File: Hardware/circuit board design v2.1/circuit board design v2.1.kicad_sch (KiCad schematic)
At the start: 0 parts

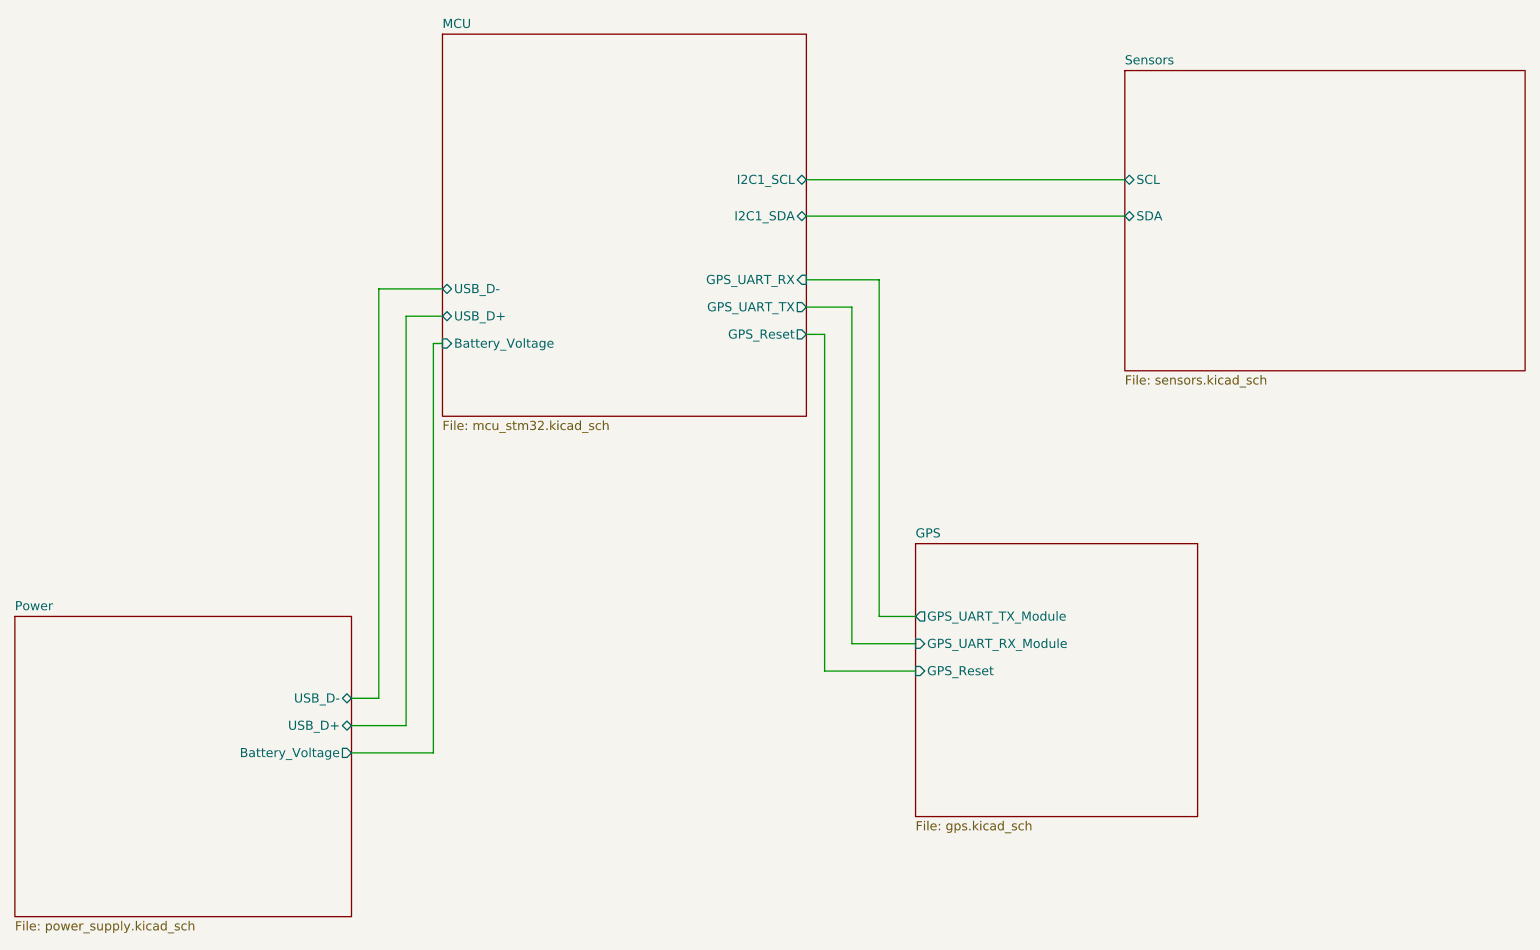
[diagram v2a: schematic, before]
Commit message: Added interupt pins to from BMI088 and LIS
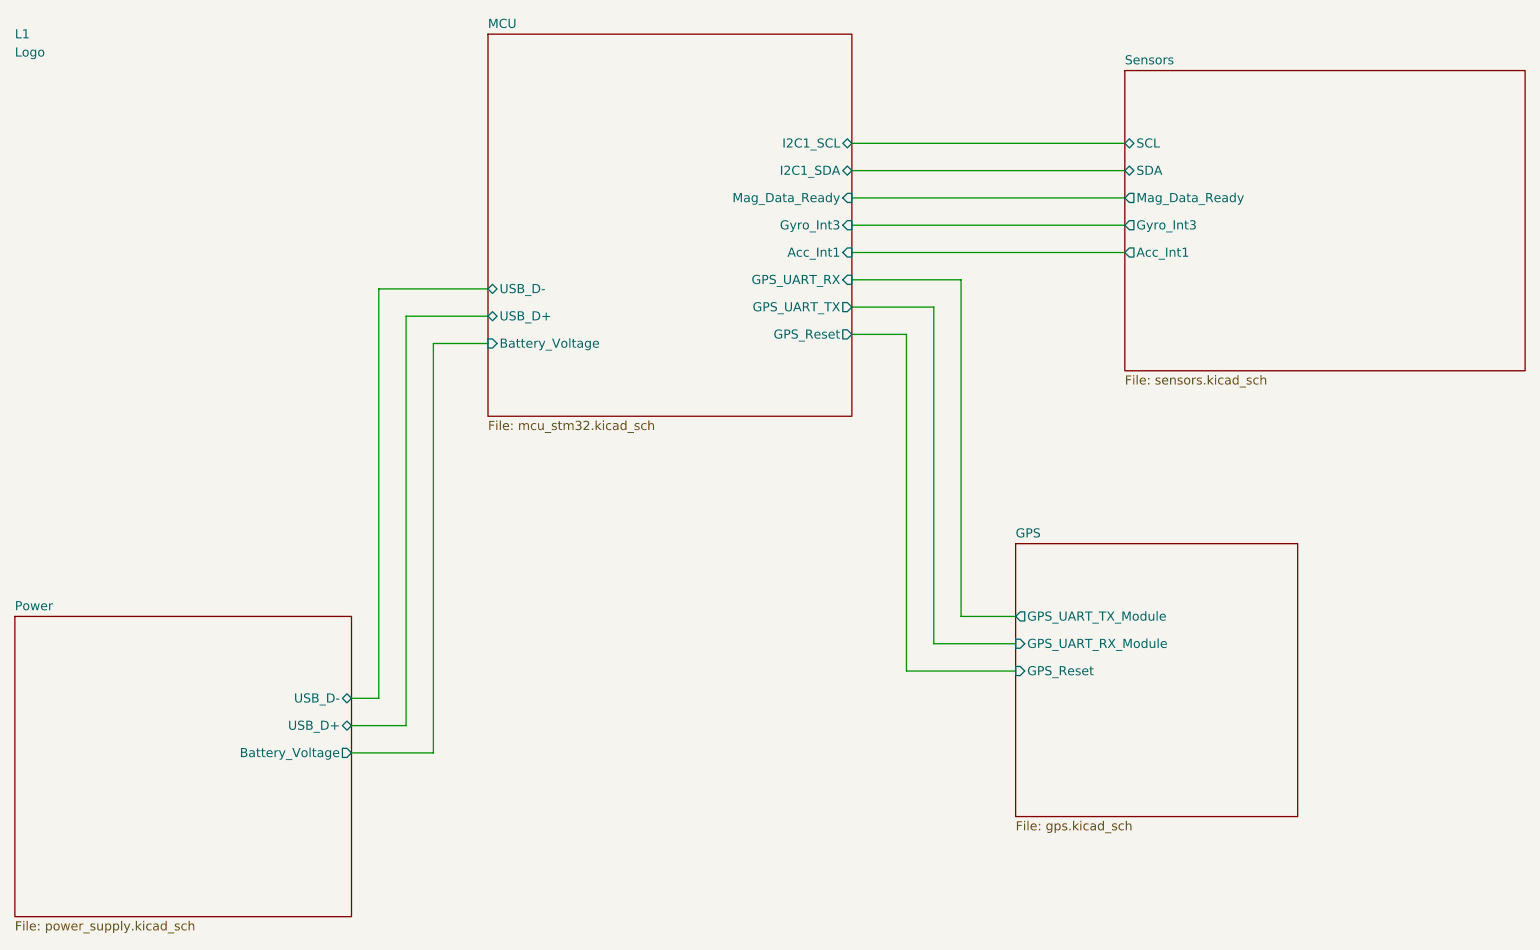
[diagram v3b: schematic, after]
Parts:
- added L1: Logo, Components:ICSS_Logo, symbol Components:Logo
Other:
- sheet MCU ports: added Acc_Int1, Gyro_Int3, Mag_Data_Ready; removed none
- sheet Sensors ports: added Acc_Int1, Gyro_Int3, Mag_Data_Ready; removed none
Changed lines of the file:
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@@
     (stroke (width 0) (type default) (color 0 0 0 0))
   )
-  (wire (pts (xy 144.78 74.93) (xy 144.78 121.92))
-    (stroke (width 0) (type default) (color 0 0 0 0))
-  )
-  (wire (pts (xy 91.44 72.39) (xy 86.36 72.39))
-    (stroke (width 0) (type default) (color 0 0 0 0))
-  )
-  (wire (pts (xy 82.55 68.58) (xy 91.44 68.58))
-    (stroke (width 0) (type default) (color 0 0 0 0))
-  )
-  (wire (pts (xy 148.59 71.12) (xy 148.59 118.11))
+  (wire (pts (xy 156.21 74.93) (xy 156.21 121.92))
+    (stroke (width 0) (type default) (color 0 0 0 0))
+  )
+  (wire (pts (xy 97.79 72.39) (xy 86.36 72.39))
+    (stroke (width 0) (type default) (color 0 0 0 0))
+  )
+  (wire (pts (xy 82.55 68.58) (xy 97.79 68.58))
+    (stroke (width 0) (type default) (color 0 0 0 0))
+  )
+  (wire (pts (xy 160.02 71.12) (xy 160.02 118.11))
     (stroke (width 0) (type default) (color 0 0 0 0))
   )
@@
     (stroke (width 0) (type default) (color 0 0 0 0))
   )
-  (wire (pts (xy 142.24 53.34) (xy 186.69 53.34))
-    (stroke (width 0) (type default) (color 0 0 0 0))
-  )
-  (wire (pts (xy 152.4 114.3) (xy 157.48 114.3))
-    (stroke (width 0) (type default) (color 0 0 0 0))
-  )
-  (wire (pts (xy 142.24 58.42) (xy 186.69 58.42))
+  (wire (pts (xy 163.83 114.3) (xy 171.45 114.3))
     (stroke (width 0) (type default) (color 0 0 0 0))
   )
@@
     (stroke (width 0) (type default) (color 0 0 0 0))
   )
-  (wire (pts (xy 142.24 71.12) (xy 148.59 71.12))
-    (stroke (width 0) (type default) (color 0 0 0 0))
-  )
-  (wire (pts (xy 152.4 67.31) (xy 152.4 114.3))
-    (stroke (width 0) (type default) (color 0 0 0 0))
-  )
-  (wire (pts (xy 148.59 118.11) (xy 157.48 118.11))
-    (stroke (width 0) (type default) (color 0 0 0 0))
-  )
-  (wire (pts (xy 142.24 74.93) (xy 144.78 74.93))
+  (wire (pts (xy 148.59 59.69) (xy 186.69 59.69))
+    (stroke (width 0) (type default) (color 0 0 0 0))
+  )
+  (wire (pts (xy 148.59 71.12) (xy 160.02 71.12))
+    (stroke (width 0) (type default) (color 0 0 0 0))
+  )
+  (wire (pts (xy 163.83 67.31) (xy 163.83 114.3))
+    (stroke (width 0) (type default) (color 0 0 0 0))
+  )
+  (wire (pts (xy 148.59 55.88) (xy 186.69 55.88))
+    (stroke (width 0) (type default) (color 0 0 0 0))
+  )
+  (wire (pts (xy 160.02 118.11) (xy 171.45 118.11))
+    (stroke (width 0) (type default) (color 0 0 0 0))
+  )
+  (wire (pts (xy 148.59 74.93) (xy 156.21 74.93))
+    (stroke (width 0) (type default) (color 0 0 0 0))
+  )
+  (wire (pts (xy 148.59 52.07) (xy 186.69 52.07))
     (stroke (width 0) (type default) (color 0 0 0 0))
   )
@@
     (stroke (width 0) (type default) (color 0 0 0 0))
   )
-  (wire (pts (xy 142.24 67.31) (xy 152.4 67.31))
-    (stroke (width 0) (type default) (color 0 0 0 0))
-  )
-  (wire (pts (xy 90.17 76.2) (xy 91.44 76.2))
-    (stroke (width 0) (type default) (color 0 0 0 0))
-  )
-  (wire (pts (xy 144.78 121.92) (xy 157.48 121.92))
+  (wire (pts (xy 148.59 63.5) (xy 186.69 63.5))
+    (stroke (width 0) (type default) (color 0 0 0 0))
+  )
+  (wire (pts (xy 148.59 67.31) (xy 163.83 67.31))
+    (stroke (width 0) (type default) (color 0 0 0 0))
+  )
+  (wire (pts (xy 90.17 76.2) (xy 97.79 76.2))
+    (stroke (width 0) (type default) (color 0 0 0 0))
+  )
+  (wire (pts (xy 156.21 121.92) (xy 171.45 121.92))
     (stroke (width 0) (type default) (color 0 0 0 0))
   )
   (wire (pts (xy 78.74 133.35) (xy 90.17 133.35))
     (stroke (width 0) (type default) (color 0 0 0 0))
+  )
+  (wire (pts (xy 148.59 48.26) (xy 186.69 48.26))
+    (stroke (width 0) (type default) (color 0 0 0 0))
+  )
+  (symbol (lib_id "Components:Logo") (at 30.48 34.29 0) (unit 1)
+    (in_bom yes) (on_board yes) (fields_autoplaced)
+    (property "Reference" "L1" (id 0) (at 31.75 33.0199 0)
+      (effects (font (size 1.27 1.27)) (justify left))
+    )
+    (property "Value" "Logo" (id 1) (at 31.75 35.5599 0)
+      (effects (font (size 1.27 1.27)) (justify left))
+    )
+    (property "Footprint" "Components:ICSS_Logo" (id 2) (at 30.48 34.29 0)
+      (effects (font (size 1.27 1.27)) hide)
+    )
+    (property "Datasheet" "" (id 3) (at 30.48 34.29 0)
+      (effects (font (size 1.27 1.27)) hide)
+    )
   )
   (sheet (at 186.69 38.1) (size 55.88 41.91) (fields_autoplaced)
@@
       (effects (font (size 1.27 1.27)) (justify left top))
     )
-    (pin "SCL" bidirectional (at 186.69 53.34 180)
-      (effects (font (size 1.27 1.27)) (justify left))
-    )
-    (pin "SDA" bidirectional (at 186.69 58.42 180)
+    (pin "SCL" bidirectional (at 186.69 48.26 180)
+      (effects (font (size 1.27 1.27)) (justify left))
+    )
+    (pin "SDA" bidirectional (at 186.69 52.07 180)
+      (effects (font (size 1.27 1.27)) (justify left))
+    )
+    (pin "Mag_Data_Ready" output (at 186.69 55.88 180)
+      (effects (font (size 1.27 1.27)) (justify left))
+    )
+    (pin "Acc_Int1" output (at 186.69 63.5 180)
+      (effects (font (size 1.27 1.27)) (justify left))
+    )
+    (pin "Gyro_Int3" output (at 186.69 59.69 180)
       (effects (font (size 1.27 1.27)) (justify left))
     )
@@
     )
   )
-  (sheet (at 157.48 104.14) (size 39.37 38.1) (fields_autoplaced)
+  (sheet (at 171.45 104.14) (size 39.37 38.1) (fields_autoplaced)
     (stroke (width 0.1524) (type solid) (color 0 0 0 0))
     (fill (color 0 0 0 0.0000))
-    (property "Sheet name" "GPS" (id 0) (at 157.48 103.4284 0)
+    (property "Sheet name" "GPS" (id 0) (at 171.45 103.4284 0)
       (effects (font (size 1.27 1.27)) (justify left bottom))
     )
-    (property "Sheet file" "gps.kicad_sch" (id 1) (at 157.48 142.8246 0)
+    (property "Sheet file" "gps.kicad_sch" (id 1) (at 171.45 142.8246 0)
       (effects (font (size 1.27 1.27)) (justify left top))
     )
-    (pin "GPS_Reset" input (at 157.48 121.92 180)
-      (effects (font (size 1.27 1.27)) (justify left))
-    )
-    (pin "GPS_UART_TX_Module" output (at 157.48 114.3 180)
-      (effects (font (size 1.27 1.27)) (justify left))
-    )
-    (pin "GPS_UART_RX_Module" input (at 157.48 118.11 180)
-      (effects (font (size 1.27 1.27)) (justify left))
-    )
-  )
-  (sheet (at 91.44 33.02) (size 50.8 53.34) (fields_autoplaced)
+    (pin "GPS_Reset" input (at 171.45 121.92 180)
+      (effects (font (size 1.27 1.27)) (justify left))
+    )
+    (pin "GPS_UART_TX_Module" output (at 171.45 114.3 180)
+      (effects (font (size 1.27 1.27)) (justify left))
+    )
+    (pin "GPS_UART_RX_Module" input (at 171.45 118.11 180)
+      (effects (font (size 1.27 1.27)) (justify left))
+    )
+  )
+  (sheet (at 97.79 33.02) (size 50.8 53.34) (fields_autoplaced)
     (stroke (width 0.1524) (type solid) (color 0 0 0 0))
     (fill (color 0 0 0 0.0000))
-    (property "Sheet name" "MCU" (id 0) (at 91.44 32.3084 0)
+    (property "Sheet name" "MCU" (id 0) (at 97.79 32.3084 0)
       (effects (font (size 1.27 1.27)) (justify left bottom))
     )
-    (property "Sheet file" "mcu_stm32.kicad_sch" (id 1) (at 91.44 86.9446 0)
+    (property "Sheet file" "mcu_stm32.kicad_sch" (id 1) (at 97.79 86.9446 0)
       (effects (font (size 1.27 1.27)) (justify left top))
     )
-    (pin "Battery_Voltage" input (at 91.44 76.2 180)
-      (effects (font (size 1.27 1.27)) (justify left))
-    )
-    (pin "GPS_UART_RX" input (at 142.24 67.31 0)
-      (effects (font (size 1.27 1.27)) (justify right))
-    )
-    (pin "GPS_UART_TX" output (at 142.24 71.12 0)
-      (effects (font (size 1.27 1.27)) (justify right))
-    )
-    (pin "GPS_Reset" output (at 142.24 74.93 0)
-      (effects (font (size 1.27 1.27)) (justify right))
-    )
-    (pin "USB_D-" bidirectional (at 91.44 68.58 180)
-      (effects (font (size 1.27 1.27)) (justify left))
-    )
-    (pin "USB_D+" bidirectional (at 91.44 72.39 180)
-      (effects (font (size 1.27 1.27)) (justify left))
-    )
-    (pin "I2C1_SDA" bidirectional (at 142.24 58.42 0)
-      (effects (font (size 1.27 1.27)) (justify right))
-    )
-    (pin "I2C1_SCL" bidirectional (at 142.24 53.34 0)
+    (pin "Battery_Voltage" input (at 97.79 76.2 180)
+      (effects (font (size 1.27 1.27)) (justify left))
+    )
+    (pin "GPS_UART_RX" input (at 148.59 67.31 0)
+      (effects (font (size 1.27 1.27)) (justify right))
+    )
+    (pin "GPS_UART_TX" output (at 148.59 71.12 0)
+      (effects (font (size 1.27 1.27)) (justify right))
+    )
+    (pin "GPS_Reset" output (at 148.59 74.93 0)
+      (effects (font (size 1.27 1.27)) (justify right))
+    )
+    (pin "USB_D-" bidirectional (at 97.79 68.58 180)
+      (effects (font (size 1.27 1.27)) (justify left))
+    )
+    (pin "USB_D+" bidirectional (at 97.79 72.39 180)
+      (effects (font (size 1.27 1.27)) (justify left))
+    )
+    (pin "I2C1_SDA" bidirectional (at 148.59 52.07 0)
+      (effects (font (size 1.27 1.27)) (justify right))
+    )
+    (pin "I2C1_SCL" bidirectional (at 148.59 48.26 0)
+      (effects (font (size 1.27 1.27)) (justify right))
+    )
+    (pin "Acc_Int1" input (at 148.59 63.5 0)
+      (effects (font (size 1.27 1.27)) (justify right))
+    )
+    (pin "Gyro_Int3" input (at 148.59 59.69 0)
+      (effects (font (size 1.27 1.27)) (justify right))
+    )
+    (pin "Mag_Data_Ready" input (at 148.59 55.88 0)
       (effects (font (size 1.27 1.27)) (justify right))
     )
@@
   )
   (symbol_instances
-    (path "/5a4d8c5a-da32-47cd-8dfd-858fccee0cc7/73fb8e2d-3b8a-4274-b7b3-da0b75ae8f87"
-      (reference "#FLG0101") (unit 1) (value "PWR_FLAG") (footprint "")
-    )
     (path "/5a4d8c5a-da32-47cd-8dfd-858fccee0cc7/c1196ddf-17fb-4df6-8d28-69daa69a3511"
       (reference "#FLG0102") (unit 1) (value "PWR_FLAG") (footprint "")
@@
       (reference "J6") (unit 1) (value "Conn_01x02_Male") (footprint "Connector_PinHeader_2.54mm:PinHeader_1x02_P2.54mm_Vertical")
     )
+    (path "/707d4321-6a5f-431a-bddf-316d812079af"
+      (reference "L1") (unit 1) (value "Logo") (footprint "Components:ICSS_Logo")
+    )
     (path "/5a4d8c5a-da32-47cd-8dfd-858fccee0cc7/08b32fa6-29ce-46ea-a9fb-532737bcadbb"

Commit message: PCB V2.1 sent for manufacture
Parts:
- L1: now left out of the parts list
